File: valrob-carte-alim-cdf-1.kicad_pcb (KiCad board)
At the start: 4 copper layers, 87 x 57 mm, 201 parts, among them J1 USB_C_Receptacle_USB2.0_14P, J10 Conn_01x02, J11 Conn_01x02, J12 Conn_01x02, J13 Conn_01x02, J14 Conn_01x02, J15 Conn_01x02, J16 Conn_01x02, J17 Conn_01x02, J18 Conn_01x02, J19 Conn_01x02, J2 Conn_01x02, J20 Conn_01x02, J21 Conn_01x02, J22 Conn_01x02, J3 Conn_01x04_Pin, J4 Conn_01x02, J5 Conn_01x02, J6 Conn_01x02, J7 Conn_01x02, J8 Conn_01x02, J9 Conn_01x02, SW1 SW_Push, SW2 SW_Push, SW3 SW_Push, U1 SN65HVD230, U10 TPS259472A, U11 TPS259472A, U12 TPS259472A, U2 ESP32-S3-WROOM-1, U3 TLV75733PDBV, U4 TPS56A37, U5 TPS56A37, U6 TPS259472A, U7 TPS259472A, U8 TPS259472A, U9 TPS259472A

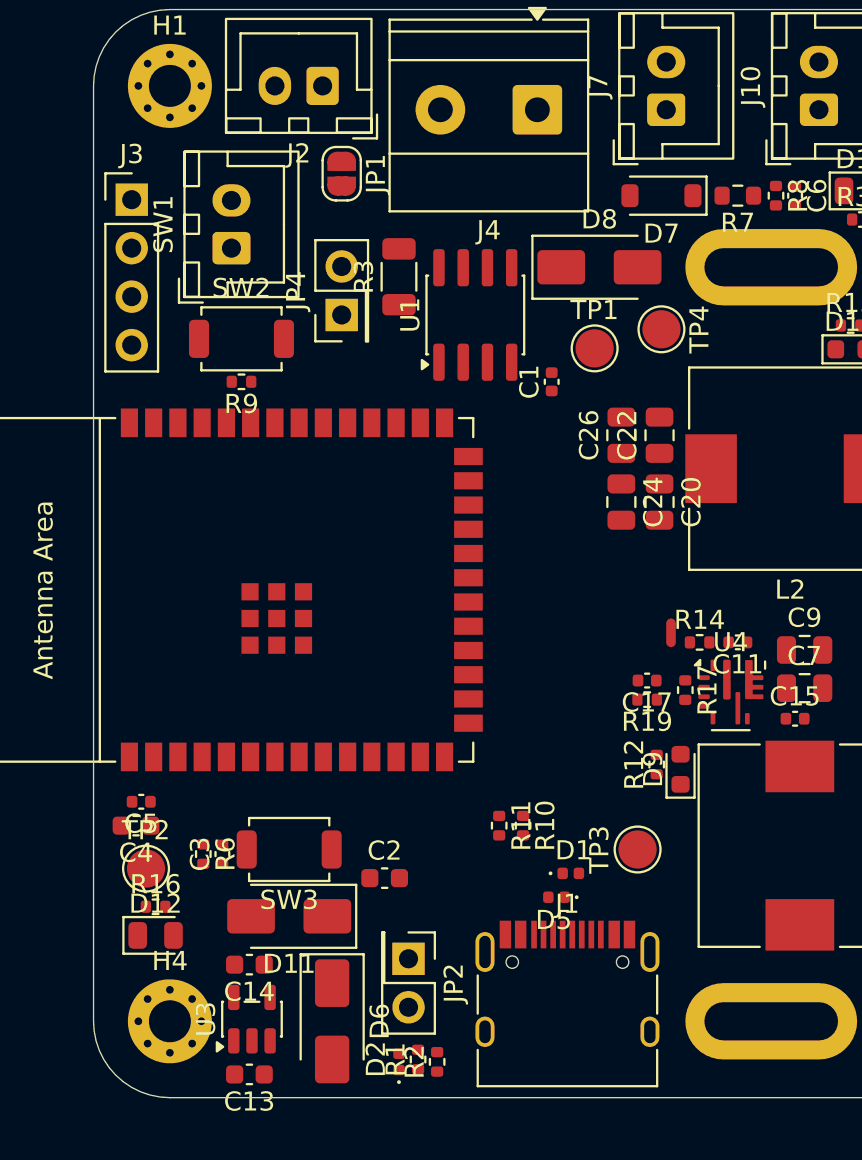
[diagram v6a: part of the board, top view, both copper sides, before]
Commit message: pcb: add can layout
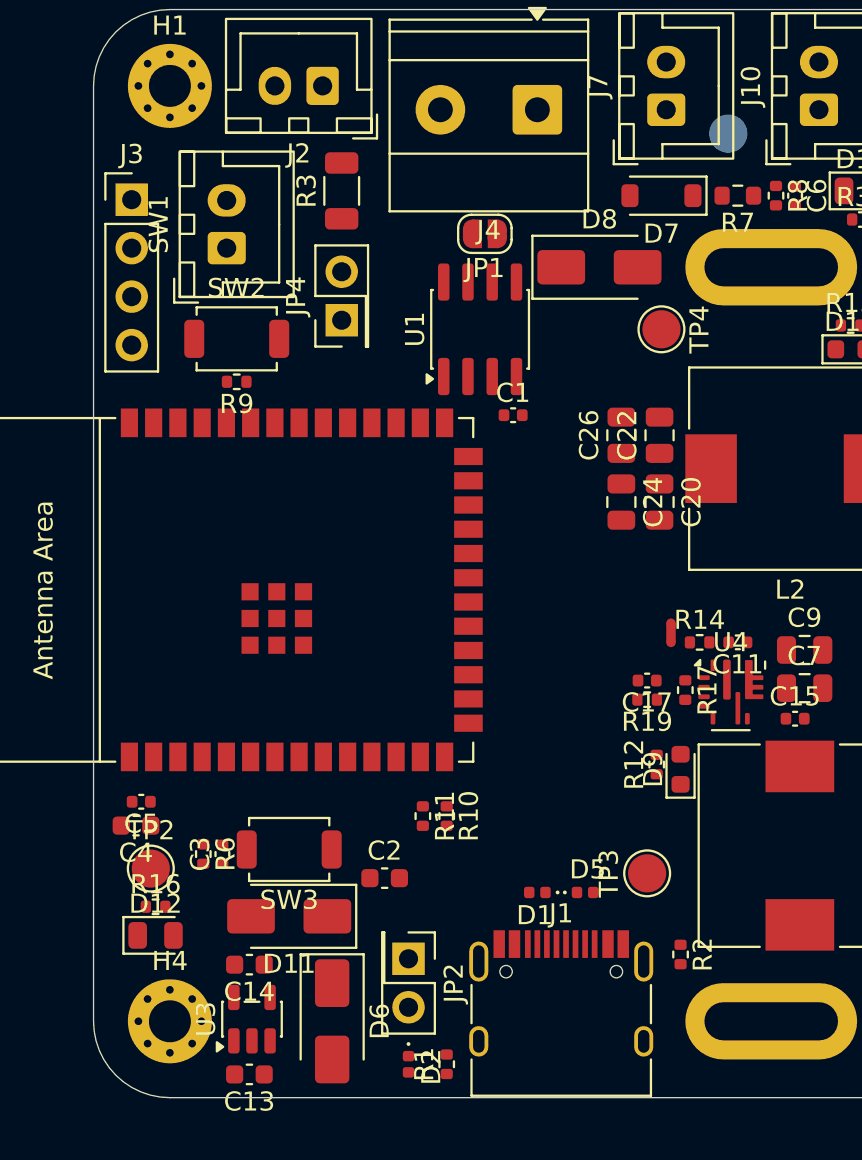
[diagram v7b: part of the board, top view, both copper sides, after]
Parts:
- TP1: moved to B.Cu
- moved R2 13.9 mm to (120.8, 102.5), turned to -90 degrees
- moved TP1 13.2 mm to (123.2, 59.5), turned to 180 degrees
- moved JP1 8.13 mm to (110.5, 64.8), turned to 180 degrees
- moved R3 5.41 mm to (103.0, 62.5)
- moved R10 4.03 mm to (108.5, 95.2)
- moved R11 4.03 mm to (107.2, 95.2)
- moved C1 2.67 mm to (112.0, 74.2), turned to 0 degrees
- moved D1 2.02 mm to (113.2, 99.2), turned to 180 degrees
- moved D5 1.52 mm to (115.8, 99.2), turned to 0 degrees
- moved R1 1.52 mm to (108.5, 108.2)
- moved TP3 1.35 mm to (119.0, 98.2)
- moved U1 0.79 mm to (110.2, 69.8)
- moved J1 0.60 mm to (114.5, 106.0)
- moved D2 0.52 mm to (106.5, 108.2), turned to -90 degrees
- moved JP4 0.28 mm to (103.0, 69.3)
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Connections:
- D2 pad 1: VBUS -> Net-(D2-K)
- D6 pad 2: Net-(D6-A) -> Net-(D2-K)
- JP2 pad 2: Net-(D6-A) -> Net-(D2-K)
- U2 pad 29: /CAN_TX -> /CAN_RX
- U2 pad 30: /CAN_RX -> /CAN_TX

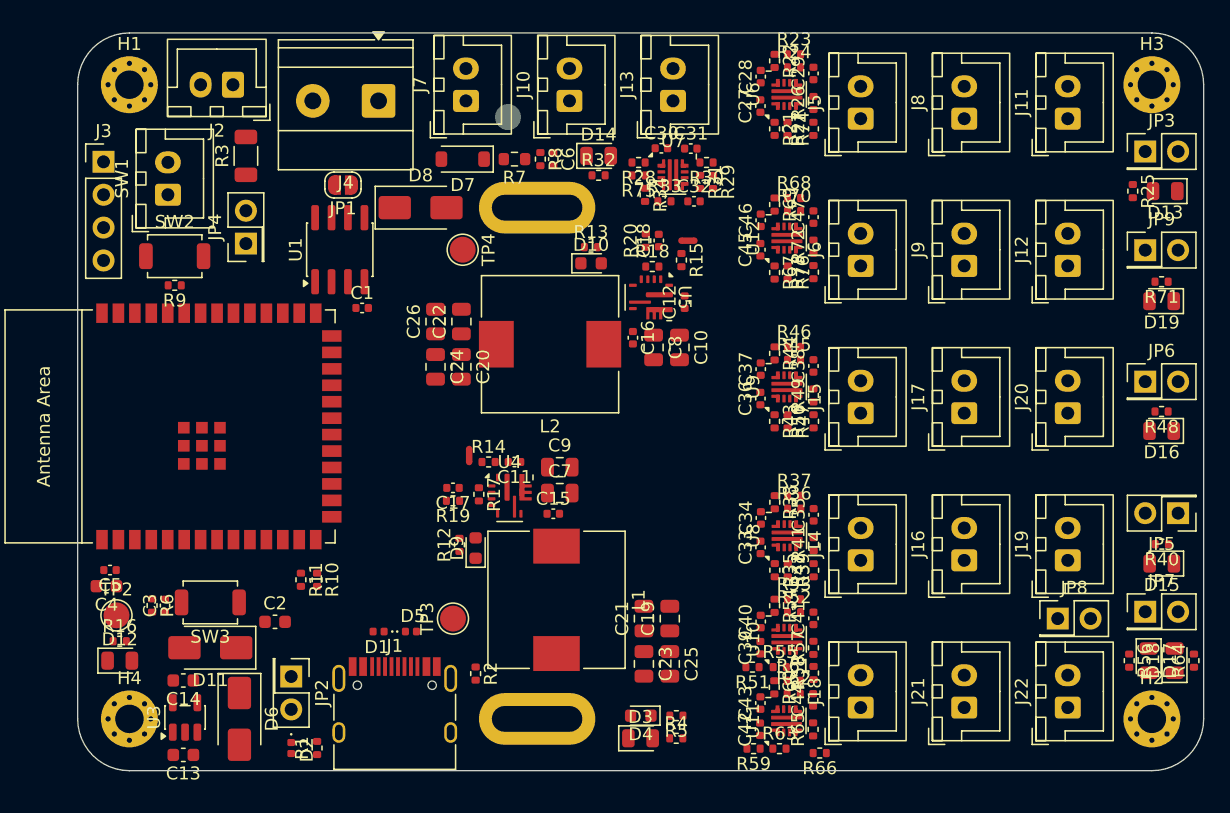
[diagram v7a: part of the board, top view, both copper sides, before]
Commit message: pcb: add gnd planes
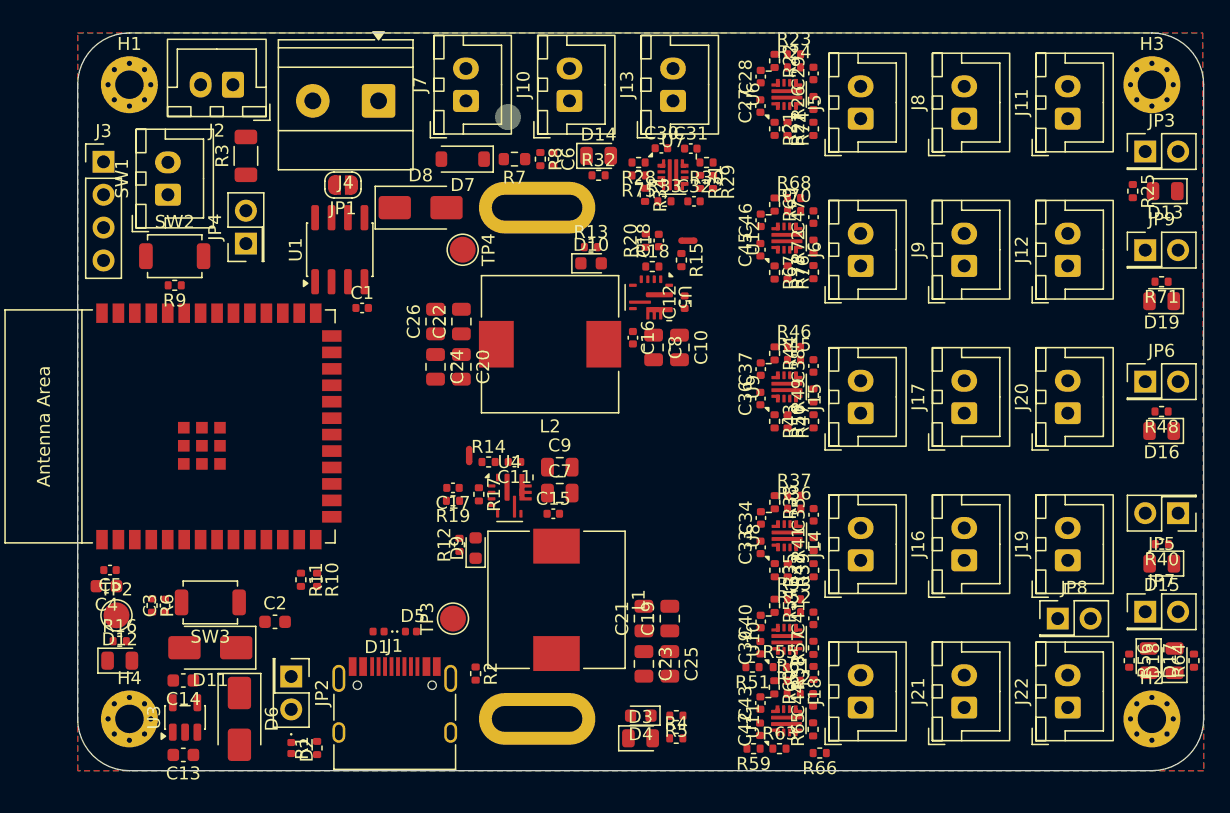
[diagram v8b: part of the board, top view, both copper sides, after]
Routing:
- added copper zone on B.Cu, net GND
- added copper zone on F.Cu, net GND
- added copper zone on In1.Cu, net GND
- added copper zone on In2.Cu, net GND
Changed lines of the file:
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@@
+		)
+	)
+	(zone
+		(net 1)
+		(net_name "GND")
+		(layers "F.Cu" "B.Cu" "In1.Cu" "In2.Cu")
+		(hatch edge 0.5)
+		(connect_pads
+			(clearance 0.2)
+		)
+		(min_thickness 0.15)
+		(filled_areas_thickness no)
+		(fill yes
+			(thermal_gap 0.35)
+			(thermal_bridge_width 0.35)
+		)
+		(polygon
+			(pts
+				(xy 90 53) (xy 176.92 53) (xy 177 110) (xy 90 110)
+			)
 		)
 	)
